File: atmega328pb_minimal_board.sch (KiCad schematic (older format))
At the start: 9 parts, among them J2 Conn_02x05_Odd_Even, J3 Conn_01x16_Male, J4 Conn_01x16_Male, U1 ATmega328PB-AU, Y1 16MHz

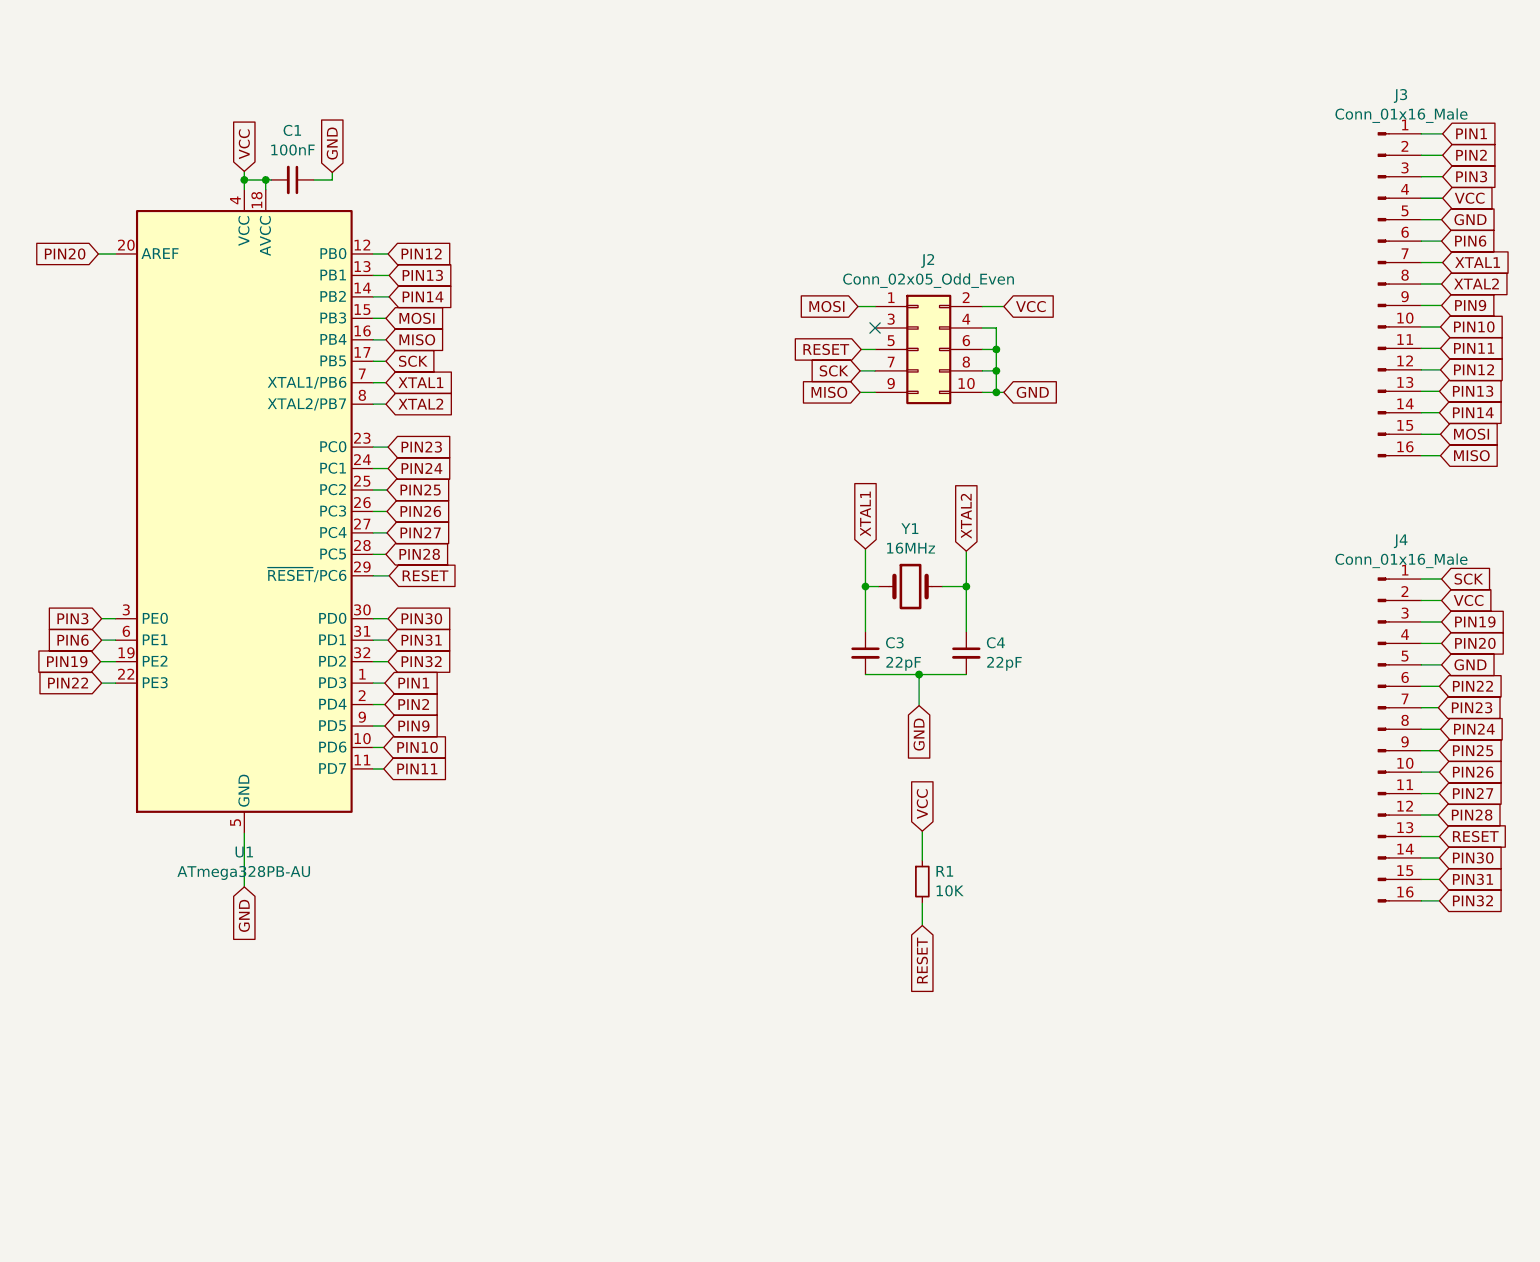
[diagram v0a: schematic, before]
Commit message: add reset button, two usart headers and an LED
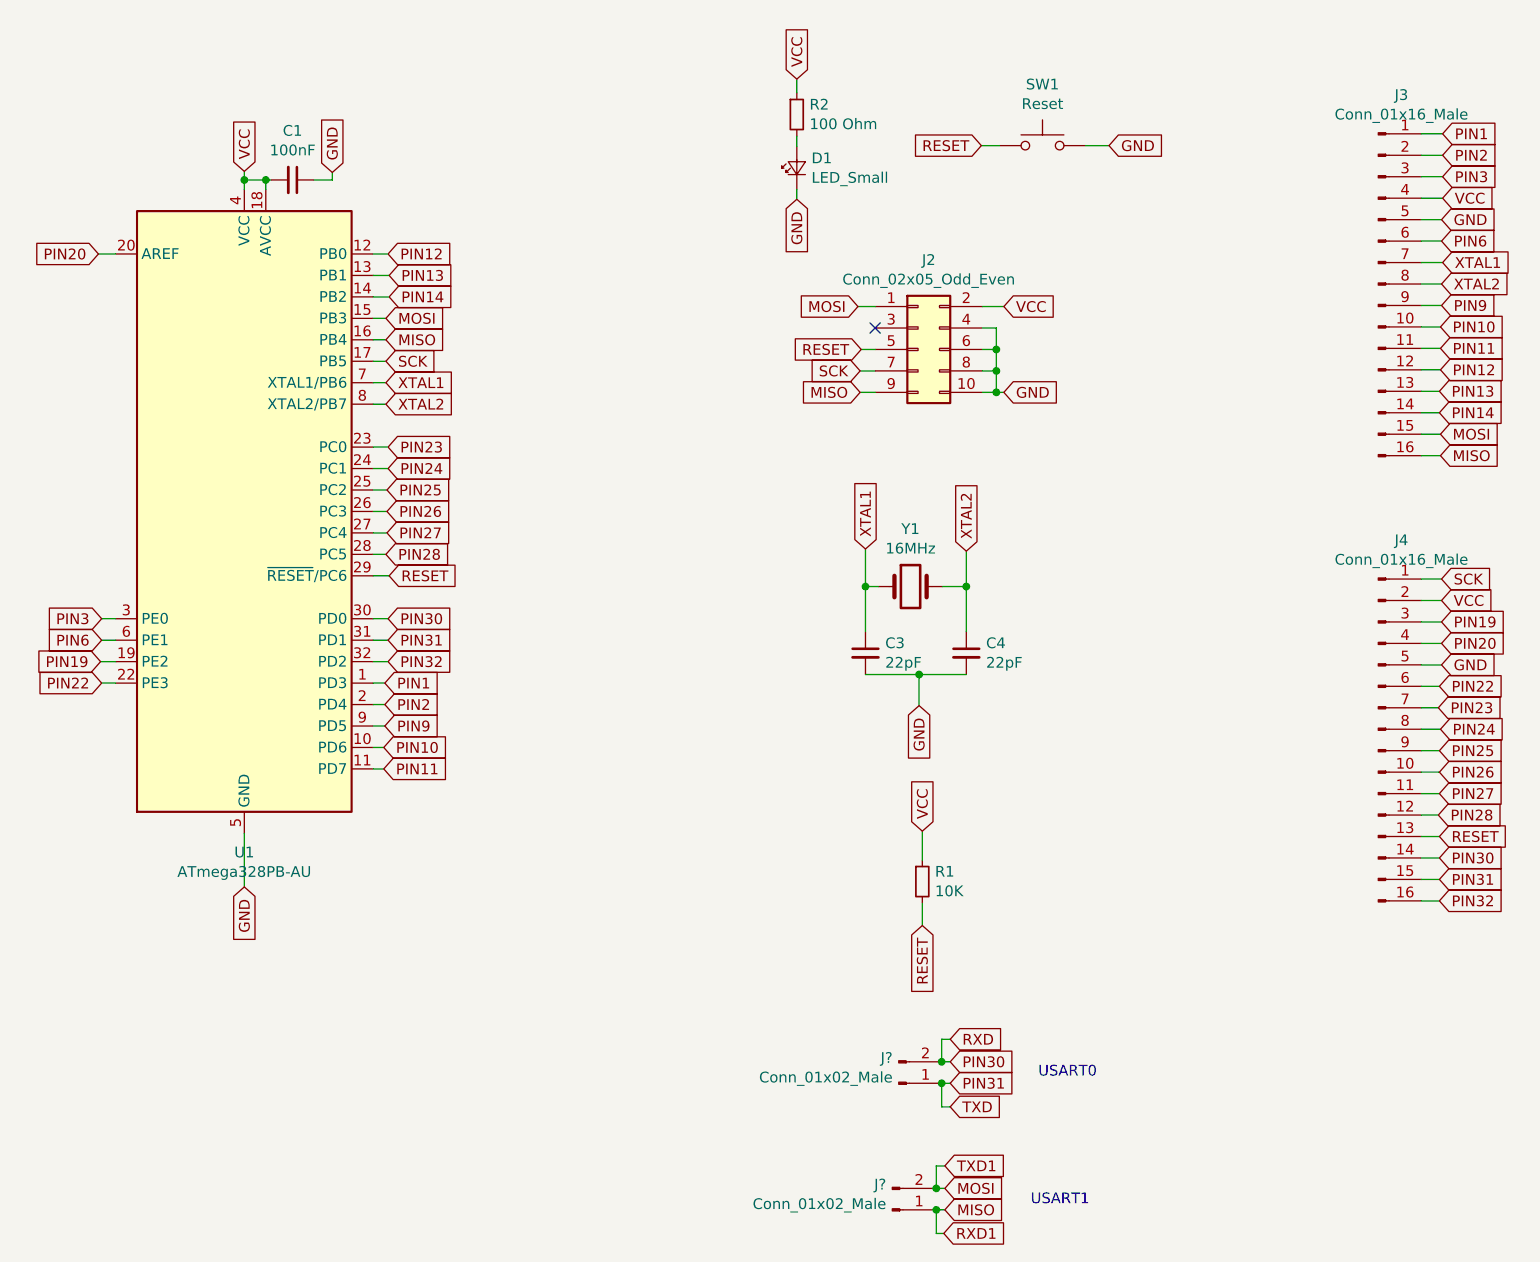
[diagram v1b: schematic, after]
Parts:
- added D1: LED_Small, LED_SMD:LED_0805_2012Metric_Pad1.15x1.40mm_HandSolder, symbol Device:LED_Small
- added J? (x2): Conn_01x02_Male, symbol Connector:Conn_01x02_Male
- added R2: 100 Ohm, Resistor_SMD:R_0805_2012Metric_Pad1.15x1.40mm_HandSolder, symbol Device:R_Small
- added SW1: Reset, Button_Switch_THT:SW_PUSH_6mm_H5mm, symbol Switch:SW_Push
- C1, C3, C4: footprint Capacitor_THT:C_Disc_D3.8mm_W2.6mm_P2.50mm -> Capacitor_SMD:C_0805_2012Metric_Pad1.15x1.40mm_HandSolder
- J3, J4: footprint Connector_PinHeader_2.54mm:PinHeader_1x16_P2.54mm_Vertical -> Connector_PinSocket_2.54mm:PinSocket_1x16_P2.54mm_Vertical
- R1: footprint Resistor_THT:R_Axial_DIN0207_L6.3mm_D2.5mm_P10.16mm_Horizontal -> Resistor_SMD:R_0805_2012Metric_Pad1.15x1.40mm_HandSolder
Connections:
- net GND: now also D1.1 (K), SW1.2
- net MISO: now also J?.1 (Pin_1)
- net MOSI: now also J?.2 (Pin_2)
- net PIN30: now also J?.2 (Pin_2)
- net PIN31: now also J?.1 (Pin_1)
- net RESET: now also SW1.1
- net VCC: now also R2.1
- new net: D1.2 (A), R2.2
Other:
- note added: "USART0"
- note added: "USART1"
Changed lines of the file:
@@
 F 0 "C3" H 7007 3631 50  0000 L CNN
 F 1 "22pF" H 7007 3540 50  0000 L CNN
-F 2 "Capacitor_THT:C_Disc_D3.8mm_W2.6mm_P2.50mm" H 6915 3585 50  0001 C CNN
+F 2 "Capacitor_SMD:C_0805_2012Metric_Pad1.15x1.40mm_HandSolder" H 6915 3585 50  0001 C CNN
 F 3 "~" H 6915 3585 50  0001 C CNN
 	1    6915 3585
@@
 F 0 "C4" H 7477 3631 50  0000 L CNN
 F 1 "22pF" H 7477 3540 50  0000 L CNN
-F 2 "Capacitor_THT:C_Disc_D3.8mm_W2.6mm_P2.50mm" H 7385 3585 50  0001 C CNN
+F 2 "Capacitor_SMD:C_0805_2012Metric_Pad1.15x1.40mm_HandSolder" H 7385 3585 50  0001 C CNN
 F 3 "~" H 7385 3585 50  0001 C CNN
 	1    7385 3585
@@
 F 0 "R1" H 7239 4696 50  0000 L CNN
 F 1 "10K" H 7239 4605 50  0000 L CNN
-F 2 "Resistor_THT:R_Axial_DIN0207_L6.3mm_D2.5mm_P10.16mm_Horizontal" H 7180 4650 50  0001 C CNN
+F 2 "Resistor_SMD:R_0805_2012Metric_Pad1.15x1.40mm_HandSolder" H 7180 4650 50  0001 C CNN
 F 3 "~" H 7180 4650 50  0001 C CNN
 	1    7180 4650
@@
 F 0 "C1" V 4016 1380 50  0000 C CNN
 F 1 "100nF" V 4107 1380 50  0000 C CNN
-F 2 "Capacitor_THT:C_Disc_D3.8mm_W2.6mm_P2.50mm" H 4245 1380 50  0001 C CNN
+F 2 "Capacitor_SMD:C_0805_2012Metric_Pad1.15x1.40mm_HandSolder" H 4245 1380 50  0001 C CNN
 F 3 "~" H 4245 1380 50  0001 C CNN
 	1    4245 1380
@@
 F 0 "J3" H 9413 2746 50  0000 C CNN
 F 1 "Conn_01x16_Male" H 9413 2655 50  0000 C CNN
-F 2 "Connector_PinHeader_2.54mm:PinHeader_1x16_P2.54mm_Vertical" H 9305 1865 50  0001 C CNN
+F 2 "Connector_PinSocket_2.54mm:PinSocket_1x16_P2.54mm_Vertical" H 9305 1865 50  0001 C CNN
 F 3 "~" H 9305 1865 50  0001 C CNN
 	1    9305 1865
@@
 F 0 "J4" H 9413 4821 50  0000 C CNN
 F 1 "Conn_01x16_Male" H 9413 4730 50  0000 C CNN
-F 2 "Connector_PinHeader_2.54mm:PinHeader_1x16_P2.54mm_Vertical" H 9305 3940 50  0001 C CNN
+F 2 "Connector_PinSocket_2.54mm:PinSocket_1x16_P2.54mm_Vertical" H 9305 3940 50  0001 C CNN
 F 3 "~" H 9305 3940 50  0001 C CNN
 	1    9305 3940
@@
 Wire Wire Line
 	9505 4740 9590 4740
+Text GLabel 6595 910  1    50   Input ~ 0
+VCC
+Text GLabel 6595 1470 3    50   Input ~ 0
+GND
+$Comp
+L Device:R_Small R2
+U 1 1 5D7069A7
+P 6595 1075
+F 0 "R2" H 6654 1121 50  0000 L CNN
+F 1 "100 Ohm" H 6654 1030 50  0000 L CNN
+F 2 "Resistor_SMD:R_0805_2012Metric_Pad1.15x1.40mm_HandSolder" H 6595 1075 50  0001 C CNN
+F 3 "~" H 6595 1075 50  0001 C CNN
+	1    6595 1075
+	1    0    0    -1
+$EndComp
+$Comp
+L Device:LED_Small D1
+U 1 1 5D706EDE
+P 6595 1325
+F 0 "D1" V 6641 1257 50  0000 R CNN
+F 1 "LED_Small" V 6550 1257 50  0000 R CNN
+F 2 "LED_SMD:LED_0805_2012Metric_Pad1.15x1.40mm_HandSolder" V 6595 1325 50  0001 C CNN
+F 3 "~" V 6595 1325 50  0001 C CNN
+	1    6595 1325
+	0    -1   -1   0
+$EndComp
+Wire Wire Line
+	6595 1470 6595 1425
+Wire Wire Line
+	6595 1225 6595 1175
+Wire Wire Line
+	6595 910  6595 975
+$Comp
+L Switch:SW_Push SW1
+U 1 1 5D71343A
+P 7740 1220
+F 0 "SW1" H 7740 1505 50  0000 C CNN
+F 1 "Reset" H 7740 1414 50  0000 C CNN
+F 2 "Button_Switch_THT:SW_PUSH_6mm_H5mm" H 7740 1420 50  0001 C CNN
+F 3 "~" H 7740 1420 50  0001 C CNN
+	1    7740 1220
+	1    0    0    -1
+$EndComp
+Text GLabel 7455 1220 0    50   Input ~ 0
+RESET
+Wire Wire Line
+	7455 1220 7540 1220
+Text GLabel 8050 1220 2    50   Input ~ 0
+GND
+Wire Wire Line
+	8050 1220 7940 1220
+$Comp
+L Connector:Conn_01x02_Male J?
+U 1 1 5D72459C
+P 7070 5590
+F 0 "J?" H 7042 5472 50  0000 R CNN
+F 1 "Conn_01x02_Male" H 7042 5563 50  0000 R CNN
+F 2 "" H 7070 5590 50  0001 C CNN
+F 3 "~" H 7070 5590 50  0001 C CNN
+	1    7070 5590
+	1    0    0    1
+$EndComp
+$Comp
+L Connector:Conn_01x02_Male J?
+U 1 1 5D727F44
+P 7040 6180
+F 0 "J?" H 7012 6062 50  0000 R CNN
+F 1 "Conn_01x02_Male" H 7012 6153 50  0000 R CNN
+F 2 "" H 7040 6180 50  0001 C CNN
+F 3 "~" H 7040 6180 50  0001 C CNN
+	1    7040 6180
+	1    0    0    1
+$EndComp
+Text GLabel 7310 5490 2    50   Input ~ 0
+PIN30
+Text GLabel 7310 5590 2    50   Input ~ 0
+PIN31
+Text GLabel 7285 6180 2    50   Input ~ 0
+MISO
+Text GLabel 7285 6080 2    50   Input ~ 0
+MOSI
+Wire Wire Line
+	7240 6080 7245 6080
+Wire Wire Line
+	7240 6180 7245 6180
+Text Notes 7720 5570 0    50   ~ 0
+USART0
+Text Notes 7685 6165 0    50   ~ 0
+USART1
+Text GLabel 7310 5385 2    50   Input ~ 0
+RXD
+Text GLabel 7310 5700 2    50   Input ~ 0
+TXD
+Text GLabel 7285 5975 2    50   Input ~ 0
+TXD1
+Text GLabel 7280 6290 2    50   Input ~ 0
+RXD1
+Wire Wire Line
+	7285 5975 7245 5975
+Wire Wire Line
+	7245 5975 7245 6080
+Connection ~ 7245 6080
+Wire Wire Line
+	7245 6080 7285 6080
+Wire Wire Line
+	7245 6180 7245 6290
+Wire Wire Line
+	7245 6290 7280 6290
+Connection ~ 7245 6180
+Wire Wire Line
+	7245 6180 7285 6180
+Wire Wire Line
+	7270 5490 7310 5490
+Wire Wire Line
+	7270 5590 7310 5590
+Wire Wire Line
+	7270 5385 7270 5490
+Wire Wire Line
+	7270 5385 7310 5385
+Connection ~ 7270 5490
+Wire Wire Line
+	7270 5590 7270 5700
+Wire Wire Line
+	7270 5700 7310 5700
+Connection ~ 7270 5590
 $EndSCHEMATC

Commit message: change 2 1x16 male pin headers to female connectors
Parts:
- J1, J5: renamed from J?; footprint (none) -> Connector_PinHeader_2.54mm:PinHeader_1x02_P2.54mm_Vertical
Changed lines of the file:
@@
 	8050 1220 7940 1220
 $Comp
-L Connector:Conn_01x02_Male J?
+L Connector:Conn_01x02_Male J5
 U 1 1 5D72459C
 P 7070 5590
-F 0 "J?" H 7042 5472 50  0000 R CNN
+F 0 "J5" H 7042 5472 50  0000 R CNN
 F 1 "Conn_01x02_Male" H 7042 5563 50  0000 R CNN
-F 2 "" H 7070 5590 50  0001 C CNN
+F 2 "Connector_PinHeader_2.54mm:PinHeader_1x02_P2.54mm_Vertical" H 7070 5590 50  0001 C CNN
 F 3 "~" H 7070 5590 50  0001 C CNN
 	1    7070 5590
@@
 $EndComp
 $Comp
-L Connector:Conn_01x02_Male J?
+L Connector:Conn_01x02_Male J1
 U 1 1 5D727F44
 P 7040 6180
-F 0 "J?" H 7012 6062 50  0000 R CNN
+F 0 "J1" H 7012 6062 50  0000 R CNN
 F 1 "Conn_01x02_Male" H 7012 6153 50  0000 R CNN
-F 2 "" H 7040 6180 50  0001 C CNN
+F 2 "Connector_PinHeader_2.54mm:PinHeader_1x02_P2.54mm_Vertical" H 7040 6180 50  0001 C CNN
 F 3 "~" H 7040 6180 50  0001 C CNN
 	1    7040 6180
